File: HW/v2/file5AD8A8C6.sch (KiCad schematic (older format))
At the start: 59 parts, among them J6 DUT+, J7 DUT-, J8 Remote_sense, Q4 STW45NM50, U10 Temp amp, U11 LM35, U2 TL431A, U3 ADS1115, U4 Gate DRV, U5 Volt buffer, U6 Current amp, U7 Volt sense, U8 MCP4725, U9 AD8628

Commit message: layout
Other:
- moved on the sheet: C19, R25, R26, U10, U11
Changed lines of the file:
@@
 LIBS:contrib
 LIBS:valves
-LIBS:Peters
-LIBS:BLUEPILL
 LIBS:v2-cache
 EELAYER 25 0
@@
 L C C19
 U 1 1 5ADA6D72
-P 16950 3550
-F 0 "C19" H 16975 3650 50  0000 L CNN
-F 1 "0.1u" H 16975 3450 50  0000 L CNN
-F 2 "Capacitors_SMD:C_0805_HandSoldering" H 16988 3400 50  0001 C CNN
-F 3 "" H 16950 3550 50  0001 C CNN
-	1    16950 3550
+P 9900 2050
+F 0 "C19" H 9925 2150 50  0000 L CNN
+F 1 "0.1u" H 9925 1950 50  0000 L CNN
+F 2 "Capacitors_SMD:C_0805_HandSoldering" H 9938 1900 50  0001 C CNN
+F 3 "" H 9900 2050 50  0001 C CNN
+	1    9900 2050
 	1    0    0    -1
 $EndComp
@@
 L +5V #PWR029
 U 1 1 5ADA6D73
-P 16950 3400
-F 0 "#PWR029" H 16950 3250 50  0001 C CNN
-F 1 "+5V" H 16950 3540 50  0000 C CNN
-F 2 "" H 16950 3400 50  0001 C CNN
-F 3 "" H 16950 3400 50  0001 C CNN
-	1    16950 3400
+P 9900 1900
+F 0 "#PWR029" H 9900 1750 50  0001 C CNN
+F 1 "+5V" H 9900 2040 50  0000 C CNN
+F 2 "" H 9900 1900 50  0001 C CNN
+F 3 "" H 9900 1900 50  0001 C CNN
+	1    9900 1900
 	1    0    0    -1
 $EndComp
@@
 L Earth #PWR031
 U 1 1 5ADA6D75
-P 16950 3700
-F 0 "#PWR031" H 16950 3450 50  0001 C CNN
-F 1 "Earth" H 16950 3550 50  0001 C CNN
-F 2 "" H 16950 3700 50  0001 C CNN
-F 3 "" H 16950 3700 50  0001 C CNN
-	1    16950 3700
+P 9900 2200
+F 0 "#PWR031" H 9900 1950 50  0001 C CNN
+F 1 "Earth" H 9900 2050 50  0001 C CNN
+F 2 "" H 9900 2200 50  0001 C CNN
+F 3 "" H 9900 2200 50  0001 C CNN
+	1    9900 2200
 	1    0    0    -1
 $EndComp
@@
 L LM35 U11
 U 1 1 5ADA6D91
-P 17800 3350
-F 0 "U11" H 17950 3450 60  0000 C CNN
-F 1 "LM35" H 17850 3550 60  0000 C CNN
-F 2 "TO_SOT_Packages_THT:TO-220-3_Vertical" H 18300 3900 60  0001 C CNN
-F 3 "" H 17800 3350 60  0001 C CNN
-	1    17800 3350
+P 10750 1850
+F 0 "U11" H 10900 1950 60  0000 C CNN
+F 1 "LM35" H 10800 2050 60  0000 C CNN
+F 2 "TO_SOT_Packages_THT:TO-220-3_Vertical" H 11250 2400 60  0001 C CNN
+F 3 "" H 10750 1850 60  0001 C CNN
+	1    10750 1850
 	1    0    0    -1
 $EndComp
@@
 L Earth #PWR043
 U 1 1 5ADA6D92
-P 17700 3800
-F 0 "#PWR043" H 17700 3550 50  0001 C CNN
-F 1 "Earth" H 17700 3650 50  0001 C CNN
-F 2 "" H 17700 3800 50  0001 C CNN
-F 3 "" H 17700 3800 50  0001 C CNN
-	1    17700 3800
+P 10650 2300
+F 0 "#PWR043" H 10650 2050 50  0001 C CNN
+F 1 "Earth" H 10650 2150 50  0001 C CNN
+F 2 "" H 10650 2300 50  0001 C CNN
+F 3 "" H 10650 2300 50  0001 C CNN
+	1    10650 2300
 	1    0    0    -1
 $EndComp
@@
 L +5V #PWR044
 U 1 1 5ADA6D93
-P 17700 2900
-F 0 "#PWR044" H 17700 2750 50  0001 C CNN
-F 1 "+5V" H 17700 3040 50  0000 C CNN
-F 2 "" H 17700 2900 50  0001 C CNN
-F 3 "" H 17700 2900 50  0001 C CNN
-	1    17700 2900
+P 10650 1400
+F 0 "#PWR044" H 10650 1250 50  0001 C CNN
+F 1 "+5V" H 10650 1540 50  0000 C CNN
+F 2 "" H 10650 1400 50  0001 C CNN
+F 3 "" H 10650 1400 50  0001 C CNN
+	1    10650 1400
 	1    0    0    -1
 $EndComp
@@
 L +5V #PWR045
 U 1 1 5ADA6D95
-P 16500 2850
-F 0 "#PWR045" H 16500 2700 50  0001 C CNN
-F 1 "+5V" H 16500 2990 50  0000 C CNN
-F 2 "" H 16500 2850 50  0001 C CNN
-F 3 "" H 16500 2850 50  0001 C CNN
-	1    16500 2850
+P 9450 1350
+F 0 "#PWR045" H 9450 1200 50  0001 C CNN
+F 1 "+5V" H 9450 1490 50  0000 C CNN
+F 2 "" H 9450 1350 50  0001 C CNN
+F 3 "" H 9450 1350 50  0001 C CNN
+	1    9450 1350
 	1    0    0    -1
 $EndComp
@@
 L Earth #PWR046
 U 1 1 5ADA6D96
-P 16500 3650
-F 0 "#PWR046" H 16500 3400 50  0001 C CNN
-F 1 "Earth" H 16500 3500 50  0001 C CNN
-F 2 "" H 16500 3650 50  0001 C CNN
-F 3 "" H 16500 3650 50  0001 C CNN
-	1    16500 3650
+P 9450 2150
+F 0 "#PWR046" H 9450 1900 50  0001 C CNN
+F 1 "Earth" H 9450 2000 50  0001 C CNN
+F 2 "" H 9450 2150 50  0001 C CNN
+F 3 "" H 9450 2150 50  0001 C CNN
+	1    9450 2150
 	1    0    0    -1
 $EndComp
@@
 L R R26
 U 1 1 5ADA6D97
-P 16700 4250
-F 0 "R26" V 16780 4250 50  0000 C CNN
-F 1 "10K" V 16700 4250 50  0000 C CNN
-F 2 "Resistors_SMD:R_0805_HandSoldering" V 16630 4250 50  0001 C CNN
-F 3 "" H 16700 4250 50  0001 C CNN
-	1    16700 4250
+P 9650 2750
+F 0 "R26" V 9730 2750 50  0000 C CNN
+F 1 "10K" V 9650 2750 50  0000 C CNN
+F 2 "Resistors_SMD:R_0805_HandSoldering" V 9580 2750 50  0001 C CNN
+F 3 "" H 9650 2750 50  0001 C CNN
+	1    9650 2750
 	-1   0    0    1
 $EndComp
@@
 L Earth #PWR047
 U 1 1 5ADA6D98
-P 16700 4500
-F 0 "#PWR047" H 16700 4250 50  0001 C CNN
-F 1 "Earth" H 16700 4350 50  0001 C CNN
-F 2 "" H 16700 4500 50  0001 C CNN
-F 3 "" H 16700 4500 50  0001 C CNN
-	1    16700 4500
+P 9650 3000
+F 0 "#PWR047" H 9650 2750 50  0001 C CNN
+F 1 "Earth" H 9650 2850 50  0001 C CNN
+F 2 "" H 9650 3000 50  0001 C CNN
+F 3 "" H 9650 3000 50  0001 C CNN
+	1    9650 3000
 	1    0    0    -1
 $EndComp
@@
 L R R25
 U 1 1 5ADA6D99
-P 16500 3950
-F 0 "R25" V 16580 3950 50  0000 C CNN
-F 1 "20K" V 16500 3950 50  0000 C CNN
-F 2 "Resistors_SMD:R_0805_HandSoldering" V 16430 3950 50  0001 C CNN
-F 3 "" H 16500 3950 50  0001 C CNN
-	1    16500 3950
+P 9450 2450
+F 0 "R25" V 9530 2450 50  0000 C CNN
+F 1 "20K" V 9450 2450 50  0000 C CNN
+F 2 "Resistors_SMD:R_0805_HandSoldering" V 9380 2450 50  0001 C CNN
+F 3 "" H 9450 2450 50  0001 C CNN
+	1    9450 2450
 	0    1    1    0
 $EndComp
-Text Notes 15550 3150 0    60   ~ 0
+Text Notes 8500 1650 0    60   ~ 0
 150C = 4.5V
 $Comp
@@
 Text GLabel 1100 2100 0    60   Input ~ 0
 SCL
-Text GLabel 15650 3300 0    60   Input ~ 0
+Text GLabel 8600 1800 0    60   Input ~ 0
 LoadBlockTemp
 $Comp
@@
 	5000 4550 5000 4750
 Wire Wire Line
-	17700 3050 17700 2900
-Wire Wire Line
-	16500 3000 16500 2850
-Wire Wire Line
-	16500 3650 16500 3600
-Wire Wire Line
-	16700 3400 16700 4100
-Wire Wire Line
-	16000 3950 16000 3300
-Wire Wire Line
-	15650 3300 16100 3300
-Connection ~ 16000 3300
-Wire Wire Line
-	17400 3400 17400 3200
-Wire Wire Line
-	17400 3200 16700 3200
-Wire Wire Line
-	16000 3950 16350 3950
-Wire Wire Line
-	16700 3950 16650 3950
-Connection ~ 16700 3950
-Wire Wire Line
-	16700 4500 16700 4400
+	10650 1550 10650 1400
+Wire Wire Line
+	9450 1500 9450 1350
+Wire Wire Line
+	9450 2150 9450 2100
+Wire Wire Line
+	9650 1900 9650 2600
+Wire Wire Line
+	8950 2450 8950 1800
+Wire Wire Line
+	8600 1800 9050 1800
+Connection ~ 8950 1800
+Wire Wire Line
+	10350 1900 10350 1700
+Wire Wire Line
+	10350 1700 9650 1700
+Wire Wire Line
+	8950 2450 9300 2450
+Wire Wire Line
+	9650 2450 9600 2450
+Connection ~ 9650 2450
+Wire Wire Line
+	9650 3000 9650 2900
 Wire Wire Line
 	2850 5100 2850 5100
@@
 L Earth #PWR065
 U 1 1 5ADA6DC1
-P 14850 4200
-F 0 "#PWR065" H 14850 3950 50  0001 C CNN
-F 1 "Earth" H 14850 4050 50  0001 C CNN
-F 2 "" H 14850 4200 50  0001 C CNN
-F 3 "" H 14850 4200 50  0001 C CNN
-	1    14850 4200
+P 7800 2700
+F 0 "#PWR065" H 7800 2450 50  0001 C CNN
+F 1 "Earth" H 7800 2550 50  0001 C CNN
+F 2 "" H 7800 2700 50  0001 C CNN
+F 3 "" H 7800 2700 50  0001 C CNN
+	1    7800 2700
 	1    0    0    -1
 $EndComp
@@
 L GND #PWR066
 U 1 1 5ADA6DC2
-P 15050 4200
-F 0 "#PWR066" H 15050 3950 50  0001 C CNN
-F 1 "GND" H 15050 4050 50  0000 C CNN
-F 2 "" H 15050 4200 50  0001 C CNN
-F 3 "" H 15050 4200 50  0001 C CNN
-	1    15050 4200
-	1    0    0    -1
-$EndComp
-Wire Wire Line
-	15050 4200 15050 4150
-Wire Wire Line
-	15050 4150 14850 4150
-Wire Wire Line
-	14850 4150 14850 4200
+P 8000 2700
+F 0 "#PWR066" H 8000 2450 50  0001 C CNN
+F 1 "GND" H 8000 2550 50  0000 C CNN
+F 2 "" H 8000 2700 50  0001 C CNN
+F 3 "" H 8000 2700 50  0001 C CNN
+	1    8000 2700
+	1    0    0    -1
+$EndComp
+Wire Wire Line
+	8000 2700 8000 2650
+Wire Wire Line
+	8000 2650 7800 2650
+Wire Wire Line
+	7800 2650 7800 2700
 $Comp
 L POT_TRIM RV1
@@
 L LM321 U10
 U 1 1 5ADAE55C
-P 16400 3300
-F 0 "U10" H 16400 3600 50  0000 L CNN
-F 1 "Temp amp" H 16400 3500 50  0000 L CNN
-F 2 "TO_SOT_Packages_SMD:SOT-23-5" H 16400 3300 50  0001 C CNN
-F 3 "" H 16400 3300 50  0001 C CNN
-	1    16400 3300
-	-1   0    0    1
-$EndComp
+P 9350 1800
+F 0 "U10" H 9350 2100 50  0000 L CNN
+F 1 "Temp amp" H 9350 2000 50  0000 L CNN
+F 2 "TO_SOT_Packages_SMD:SOT-23-5" H 9350 1800 50  0001 C CNN
+F 3 "" H 9350 1800 50  0001 C CNN
+	1    9350 1800
+	-1   0    0    1
+$EndComp

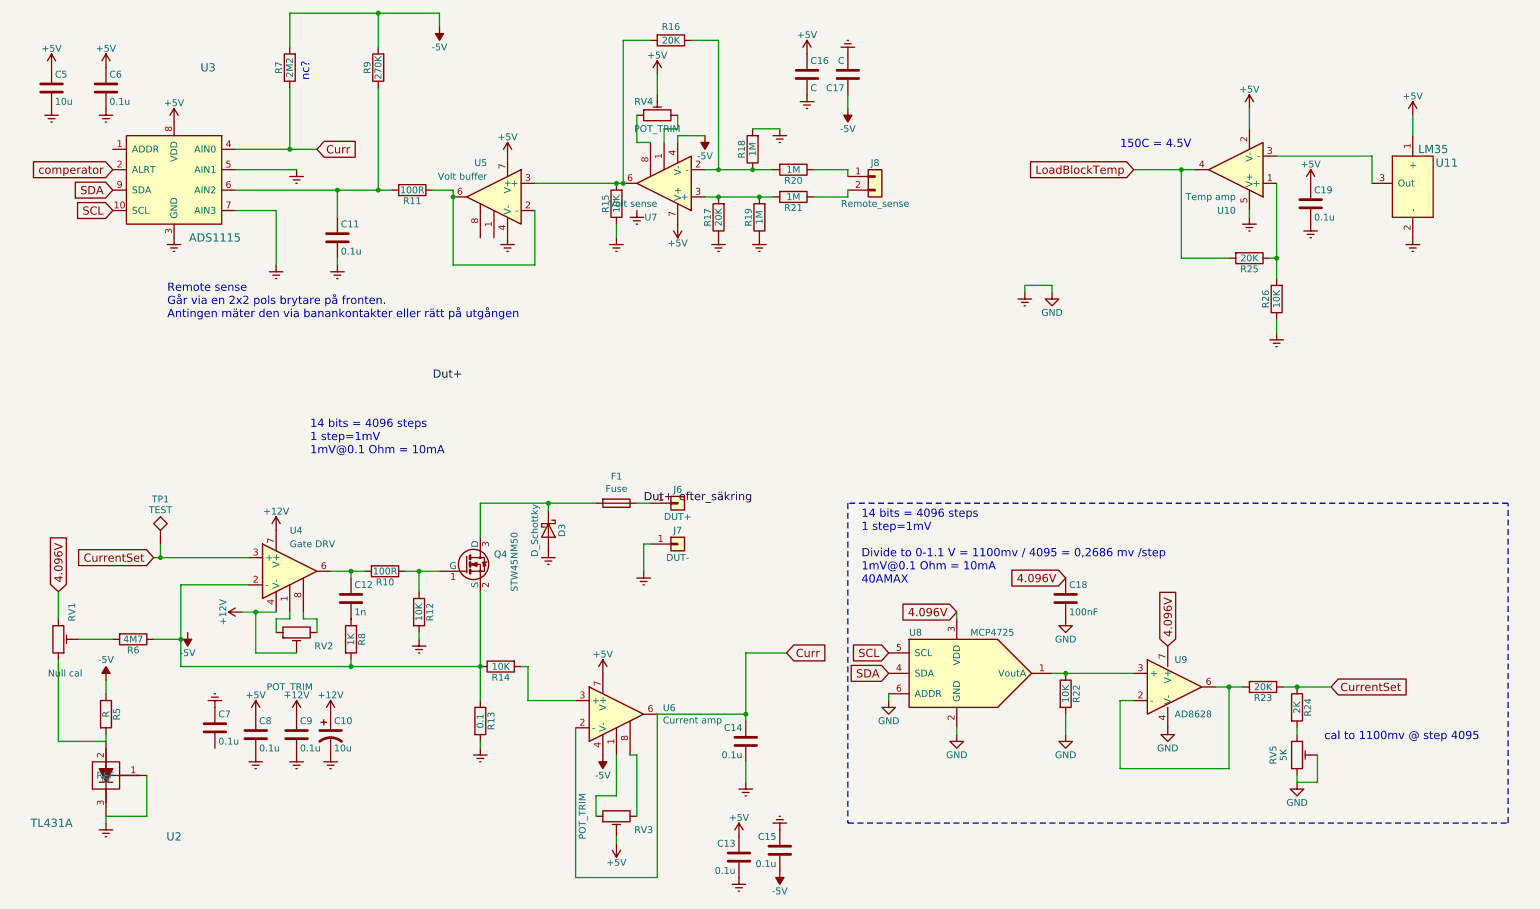
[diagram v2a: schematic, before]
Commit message: i2c pots for calibrating
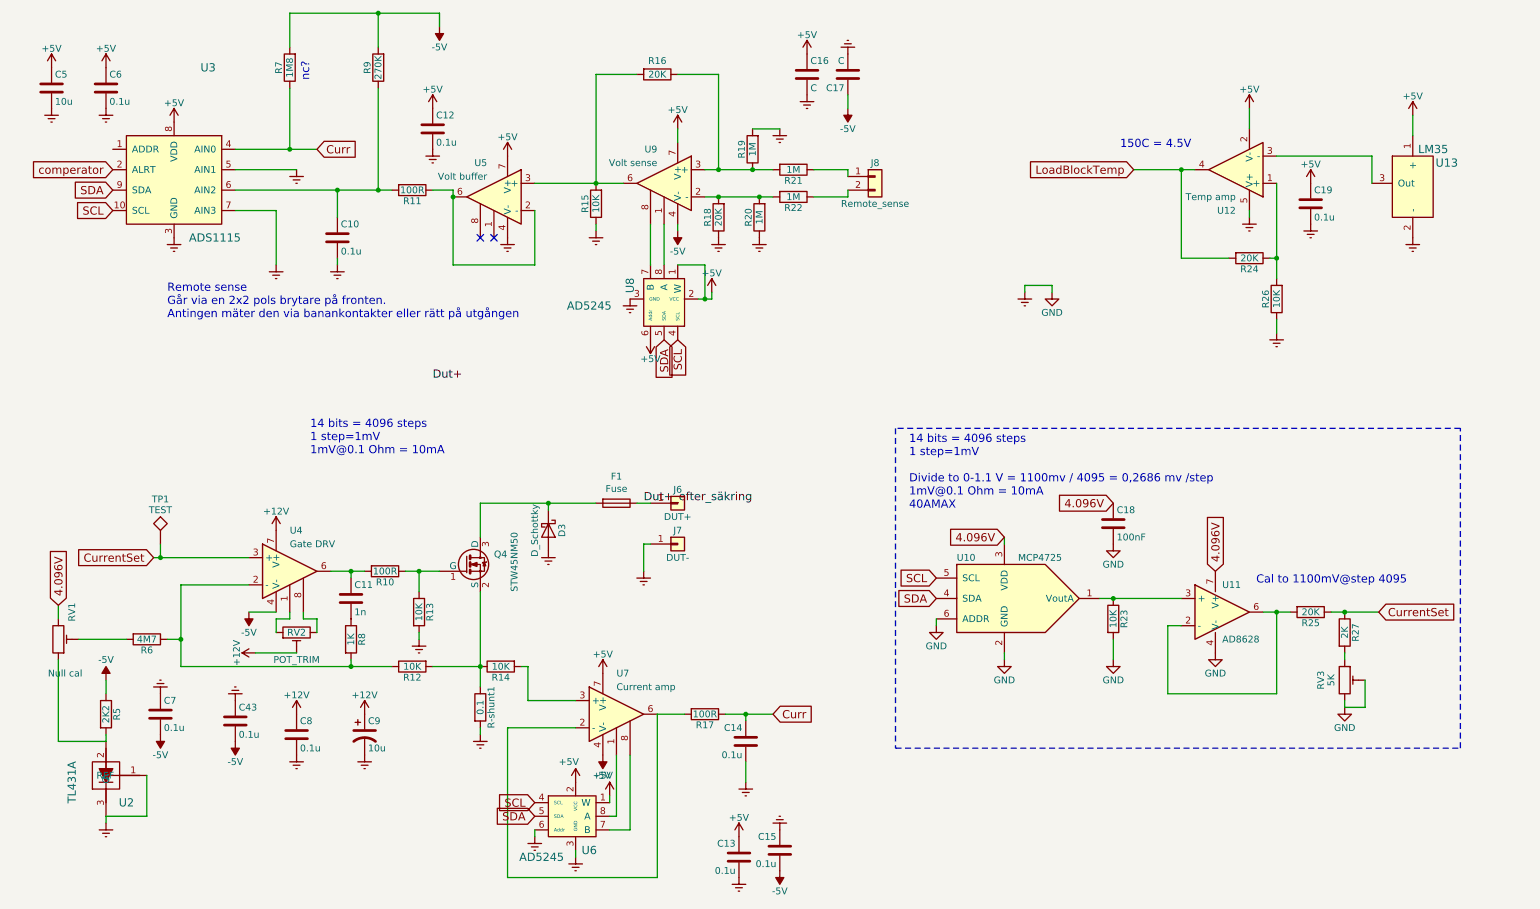
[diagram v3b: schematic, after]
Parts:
- removed RV3, RV4: POT_TRIM, Potentiometers:Potentiometer_Trimmer_ACP_CA9h2.5_Vertical_Px2.5mm_Py5.0mm, symbol POT_TRIM
- added C43: 0.1u, Capacitors_SMD:C_0805_HandSoldering, symbol C
- added R12: 10K, Resistors_SMD:R_0805_HandSoldering, symbol R
- added R17: 100R, Resistors_SMD:R_0805_HandSoldering, symbol R
- added U6, U8: AD5245, TO_SOT_Packages_SMD:SOT-23-8_Handsoldering, symbol AD5245
- Q4: footprint TO_SOT_Packages_THT:TO-247_TO-3P_Vertical -> LoadResistor:Load_mosfet
- R-shunt1: renamed from R13; footprint Resistors_THT:R_Axial_DIN0516_L15.5mm_D5.0mm_P20.32mm_Horizontal -> LoadResistor:Loadresistor
- R5: value R -> 2K2
- R7: value 2M2 -> 1M8
- renumbered C11 to C10, C12 to C11, C8 to C12, C9 to C8, C10 to C9, R12 to R13, R17 to R18, R18 to R19, R19 to R20, R20 to R21, R21 to R22, R22 to R23, R25 to R24, R23 to R25, R24 to R27, RV5 to RV3, U8 to U10, U9 to U11, U10 to U12, U11 to U13, U6 to U7, U7 to U9
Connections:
- net +12V: no longer U4.4 (V-)
- net +5V: now also U6.1 (W), U6.2 (VCC), U8.1 (W), U8.2 (VCC), U8.6 (Addr)
- net -5V: now also C7.2, U4.4 (V-), C43.2
- net Curr: now also R17.1; no longer U7.2 (-), U7.6
- net Earth: now also C43.1, U6.3 (GND), U6.6 (Addr), U8.3 (GND)
- net SCL: now also U6.4 (SCL), U8.4 (SCL)
- net SDA: now also U6.5 (SDA), U8.5 (SDA)
- net at Q4.2 (S), R-shunt1.1, R14.1: now also R12.2; no longer R6.1, R8.2, U4.2 (-)
- net at U7.1: now also U6.8 (A)
- net at U7.8: now also U6.7 (B)
- net at U9.1: now also U8.8 (A)
- net at R16.1, R19.1, R21.2: now also U9.3 (+); no longer U9.2 (-)
- net at R18.2, R20.2, R22.2: now also U9.2 (-); no longer U9.3 (+)
- net at U9.8: now also U8.7 (B)
- new net: R12.1, R6.1, R8.2, U4.2 (-)
- new net: R17.2, U7.2 (-), U7.6
- no-connect marks 0 -> 2
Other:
- note added: "Cal to 1100mV@step 4095"
- note removed: "cal to 1100mv @ step 4095"
- moved on the sheet: C12, C18, C7, C9, R-shunt1, R15, R16, R23, R25, R27, R6, RV3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

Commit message: v2 done
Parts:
- renumbered C9 to C12, C12 to C13, C13 to C14, C14 to C15, C15 to C16, C16 to C17, C17 to C18, C18 to C19, C19 to C20, C43 to C8, C8 to C9, R26 to R25, R25 to R26, U9 to U8, U8 to U9

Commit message: Before starting saturday
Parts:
- U12: symbol LM321 -> LM321-RESCUE-v2
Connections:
- net +5V: now also U12.5 (V+); no longer U12.2 (V-)
- net Earth: now also U12.2 (V-); no longer U12.5 (V+)
- net at U13.3 (Out): now also U12.1 (+); no longer U12.3 (-)
- net at R24.1, R25.2: now also U12.3 (-); no longer U12.1 (+)
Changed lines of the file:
@@
 EESchema Schematic File Version 2
+LIBS:v2-rescue
 LIBS:power
 LIBS:device
@@
 LIBS:contrib
 LIBS:valves
-LIBS:Peters
-LIBS:BLUEPILL
 LIBS:v2-cache
 EELAYER 25 0
@@
 $EndComp
 $Comp
-L LM321 U12
+L LM321-RESCUE-v2 U12
 U 1 1 5ADAE55C
 P 9350 1800
@@
 F 3 "" H 9350 1800 50  0001 C CNN
 	1    9350 1800
-	-1   0    0    1
-$EndComp
-$Comp
+	-1   0    0    -1
+$EndComp
+$Comp
